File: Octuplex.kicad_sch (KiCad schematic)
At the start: 0 parts

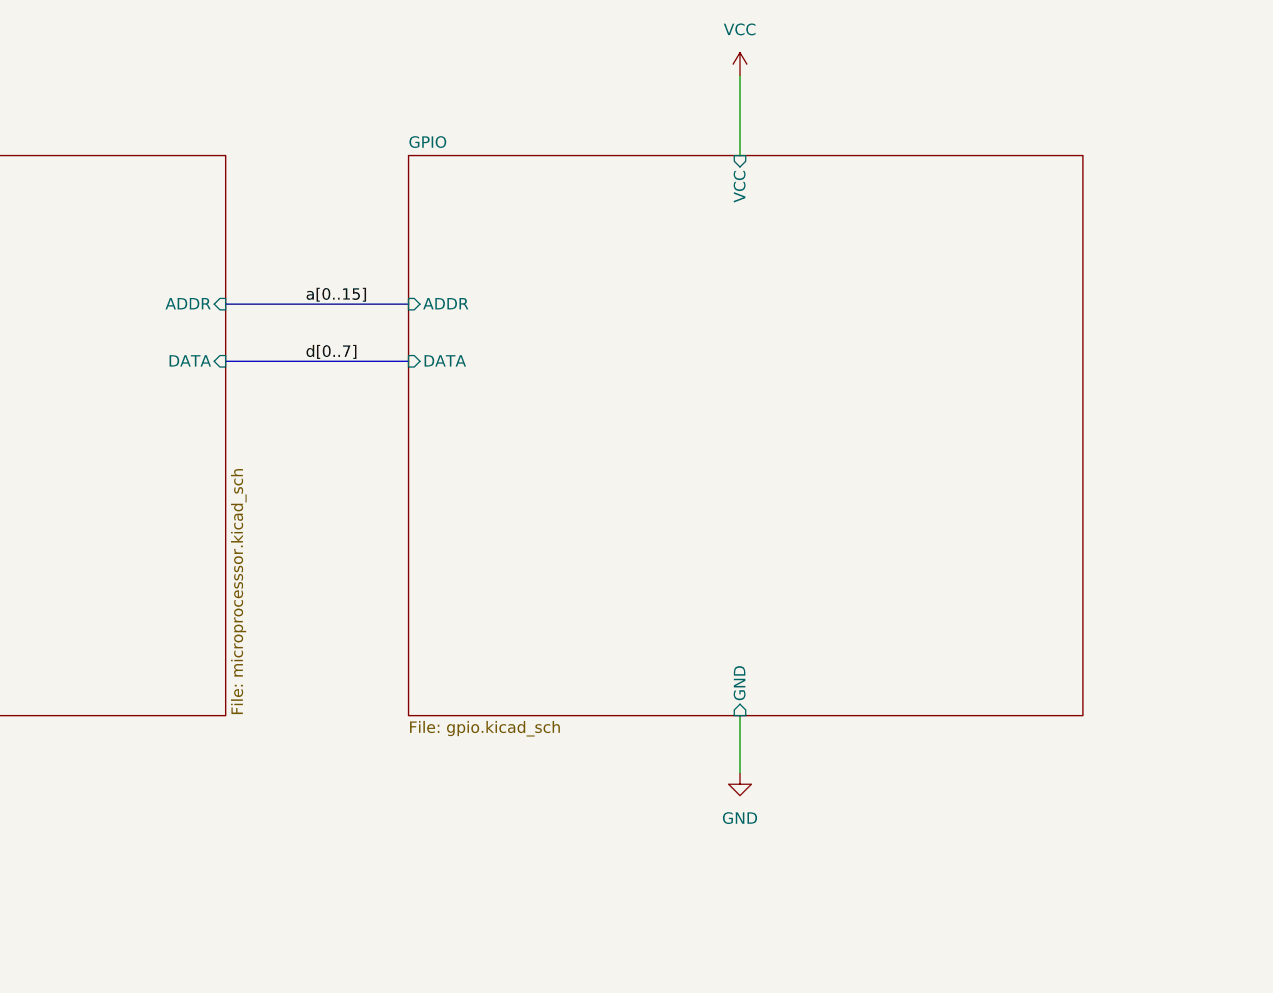
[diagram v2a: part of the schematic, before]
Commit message: Add INTS bus, address decoder, and I2C chip.
INTS bus carries RESET, NMI, FIRQ, and IRQ. Only RESET and IRQ used so far. Philips PCF8584 I2C interface chp added. Address decoder added based on 74LS139 and two 74LS138s. TODO: add CTRL bus with E, R/W, RD, and WR.
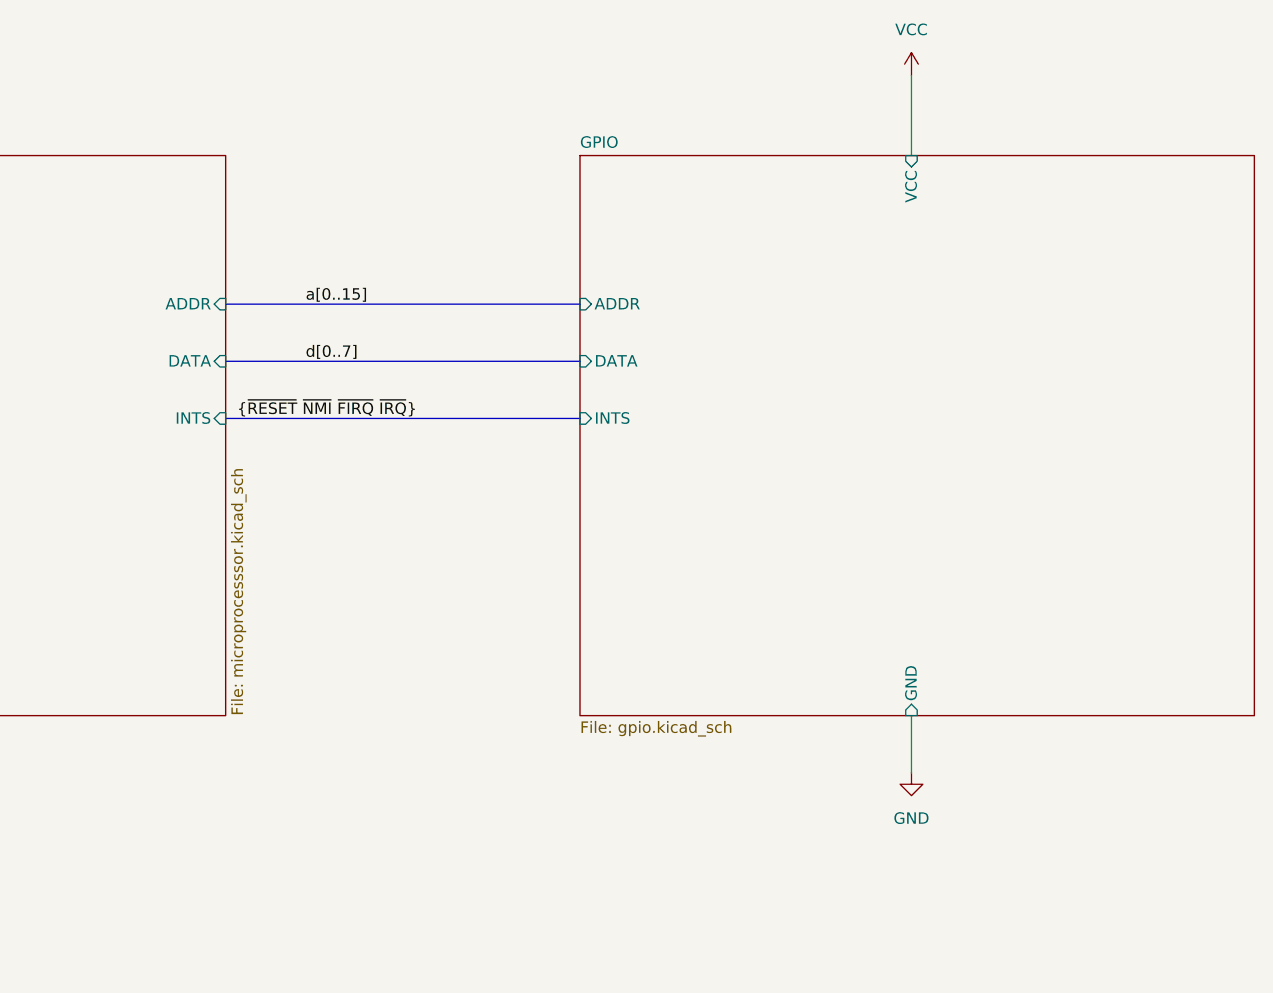
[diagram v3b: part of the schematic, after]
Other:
- sheet GPIO ports: added INTS; removed none
- sheet Microprocessor ports: added INTS; removed none
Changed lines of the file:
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@@
 	(bus
 		(pts
-			(xy 127 57.15) (xy 147.32 57.15)
+			(xy 127 57.15) (xy 166.37 57.15)
 		)
 		(stroke
@@
 	(wire
 		(pts
-			(xy 184.15 96.52) (xy 184.15 102.87)
+			(xy 203.2 96.52) (xy 203.2 102.87)
 		)
 		(stroke
@@
 	(wire
 		(pts
-			(xy 184.15 25.4) (xy 184.15 34.29)
+			(xy 203.2 25.4) (xy 203.2 34.29)
 		)
 		(stroke
@@
 	(bus
 		(pts
-			(xy 127 50.8) (xy 147.32 50.8)
+			(xy 127 50.8) (xy 166.37 50.8)
 		)
 		(stroke
@@
 		(pts
 			(xy 69.85 120.65) (xy 69.85 125.73)
+		)
+		(stroke
+			(width 0)
+			(type default)
+		)
+	)
+	(bus
+		(pts
+			(xy 127 63.5) (xy 166.37 63.5)
 		)
 		(stroke
@@
 	(label "a[0..15]"
 		(at 135.89 50.8 0)
+		(fields_autoplaced yes)
+		(effects
+			(font
+				(size 1.27 1.27)
+			)
+			(justify left bottom)
+		)
+	)
+	(label "{~{RESET} ~{NMI} ~{FIRQ} ~{IRQ}}"
+		(at 128.27 63.5 0)
 		(fields_autoplaced yes)
 		(effects
@@
 	(symbol
 		(lib_id "power:GND")
-		(at 184.15 102.87 0)
+		(at 203.2 102.87 0)
 		(unit 1)
 		(exclude_from_sim no)
@@
 		(fields_autoplaced yes)
 		(property "Reference" "#PWR036"
-			(at 184.15 109.22 0)
+			(at 203.2 109.22 0)
 			(effects
 				(font
@@
 		)
 		(property "Value" "GND"
-			(at 184.15 107.95 0)
+			(at 203.2 107.95 0)
 			(effects
 				(font
@@
 		)
 		(property "Footprint" ""
-			(at 184.15 102.87 0)
+			(at 203.2 102.87 0)
 			(effects
 				(font
@@
 		)
 		(property "Datasheet" ""
-			(at 184.15 102.87 0)
+			(at 203.2 102.87 0)
 			(effects
 				(font
@@
 		)
 		(property "Description" "Power symbol creates a global label with name \"GND\" , ground"
-			(at 184.15 102.87 0)
+			(at 203.2 102.87 0)
 			(effects
 				(font
@@
 	(symbol
 		(lib_id "power:VCC")
-		(at 184.15 25.4 0)
+		(at 203.2 25.4 0)
 		(unit 1)
 		(exclude_from_sim no)
@@
 		(fields_autoplaced yes)
 		(property "Reference" "#PWR035"
-			(at 184.15 29.21 0)
+			(at 203.2 29.21 0)
 			(effects
 				(font
@@
 		)
 		(property "Value" "VCC"
-			(at 184.15 20.32 0)
+			(at 203.2 20.32 0)
 			(effects
 				(font
@@
 		)
 		(property "Footprint" ""
-			(at 184.15 25.4 0)
+			(at 203.2 25.4 0)
 			(effects
 				(font
@@
 		)
 		(property "Datasheet" ""
-			(at 184.15 25.4 0)
+			(at 203.2 25.4 0)
 			(effects
 				(font
@@
 		)
 		(property "Description" "Power symbol creates a global label with name \"VCC\""
-			(at 184.15 25.4 0)
+			(at 203.2 25.4 0)
 			(effects
 				(font
@@
 			)
 		)
+		(pin "INTS" input
+			(at 127 63.5 0)
+			(effects
+				(font
+					(size 1.27 1.27)
+				)
+				(justify right)
+			)
+		)
 		(instances
 			(project "Octuplex"
@@
 	)
 	(sheet
-		(at 147.32 34.29)
+		(at 166.37 34.29)
 		(size 74.93 62.23)
 		(fields_autoplaced yes)
@@
 		)
 		(property "Sheetname" "GPIO"
-			(at 147.32 33.5784 0)
+			(at 166.37 33.5784 0)
 			(effects
 				(font
@@
 		)
 		(property "Sheetfile" "gpio.kicad_sch"
-			(at 147.32 97.1046 0)
+			(at 166.37 97.1046 0)
 			(effects
 				(font
@@
 		)
 		(pin "VCC" input
-			(at 184.15 34.29 90)
+			(at 203.2 34.29 90)
 			(effects
 				(font
@@
 		)
 		(pin "GND" input
-			(at 184.15 96.52 270)
+			(at 203.2 96.52 270)
 			(effects
 				(font
@@
 		)
 		(pin "DATA" input
-			(at 147.32 57.15 180)
+			(at 166.37 57.15 180)
 			(effects
 				(font
@@
 		)
 		(pin "ADDR" input
-			(at 147.32 50.8 180)
-			(effects
-				(font
+			(at 166.37 50.8 180)
+			(effects
+				(font
+					(size 1.27 1.27)
+				)
+				(justify left)
+			)
+		)
+		(pin "INTS" input
+			(at 166.37 63.5 180)
+			(effects
+				(font

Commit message: Add control bus.
R/W, E, RD, WR signals from microprocessor to GPIO.
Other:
- sheet GPIO ports: added CTRL; removed none
- sheet Microprocessor ports: added CTRL; removed none
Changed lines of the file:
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@@
+		)
+	)
+	(bus
+		(pts
+			(xy 127 69.85) (xy 166.37 69.85)
+		)
+		(stroke
+			(width 0)
+			(type default)
 		)
 	)
@@
 	(label "a[0..15]"
 		(at 135.89 50.8 0)
+		(fields_autoplaced yes)
+		(effects
+			(font
+				(size 1.27 1.27)
+			)
+			(justify left bottom)
+		)
+	)
+	(label "{R{slash}~{W} E ~{RD} ~{WR}}"
+		(at 132.08 69.85 0)
 		(fields_autoplaced yes)
 		(effects
@@
 			)
 		)
+		(pin "CTRL" input
+			(at 127 69.85 0)
+			(effects
+				(font
+					(size 1.27 1.27)
+				)
+				(justify right)
+			)
+		)
 		(instances
 			(project "Octuplex"
@@
 			(effects
 				(font
+					(size 1.27 1.27)
+				)
+				(justify left)
+			)
+		)
+		(pin "CTRL" input
+			(at 166.37 69.85 180)
+			(effects
+				(font
